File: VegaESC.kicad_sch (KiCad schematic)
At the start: 69 parts, among them J201 A, J202 B, J203 C, Q207 NTMFS5C430NLT1G, Q208 NTMFS5C430NLT1G, Q209 NTMFS5C430NLT1G, Q210 NTMFS5C430NLT1G, Q211 NTMFS5C430NLT1G, Q212 NTMFS5C430NLT1G, U201 AT32F421K8T7, U202 INA180A2, U203 FD6288Q

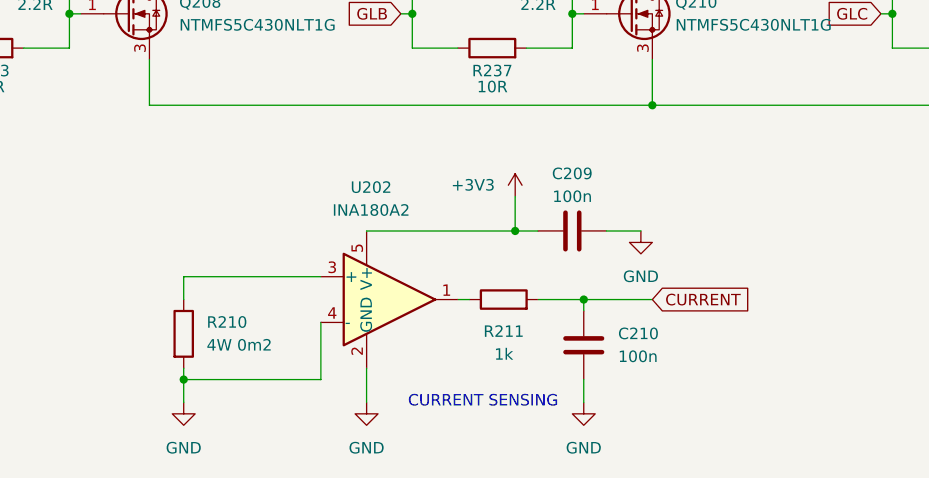
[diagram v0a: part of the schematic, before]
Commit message: esc design and current shunt resistor changes and parallel tvs diodes - still unfinished
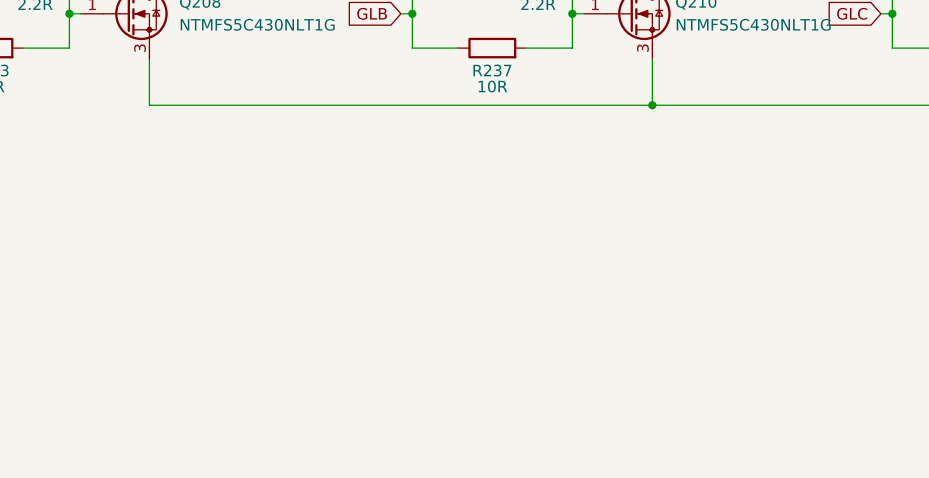
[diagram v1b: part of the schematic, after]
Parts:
- removed C209, C210: 100n, symbol Device:C
- removed R210: 4W 0m2, symbol Device:R
- removed R211: 1k, symbol Device:R
- removed U202: INA180A2, Package_TO_SOT_SMD:SOT-23-5, symbol Amplifier_Current:INA180A2
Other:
- note removed: "CURRENT SENSING"

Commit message: completed schematic design review and saved report
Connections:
- net GND: now also Q208.3 (S), Q210.3 (S), Q212.3 (S)

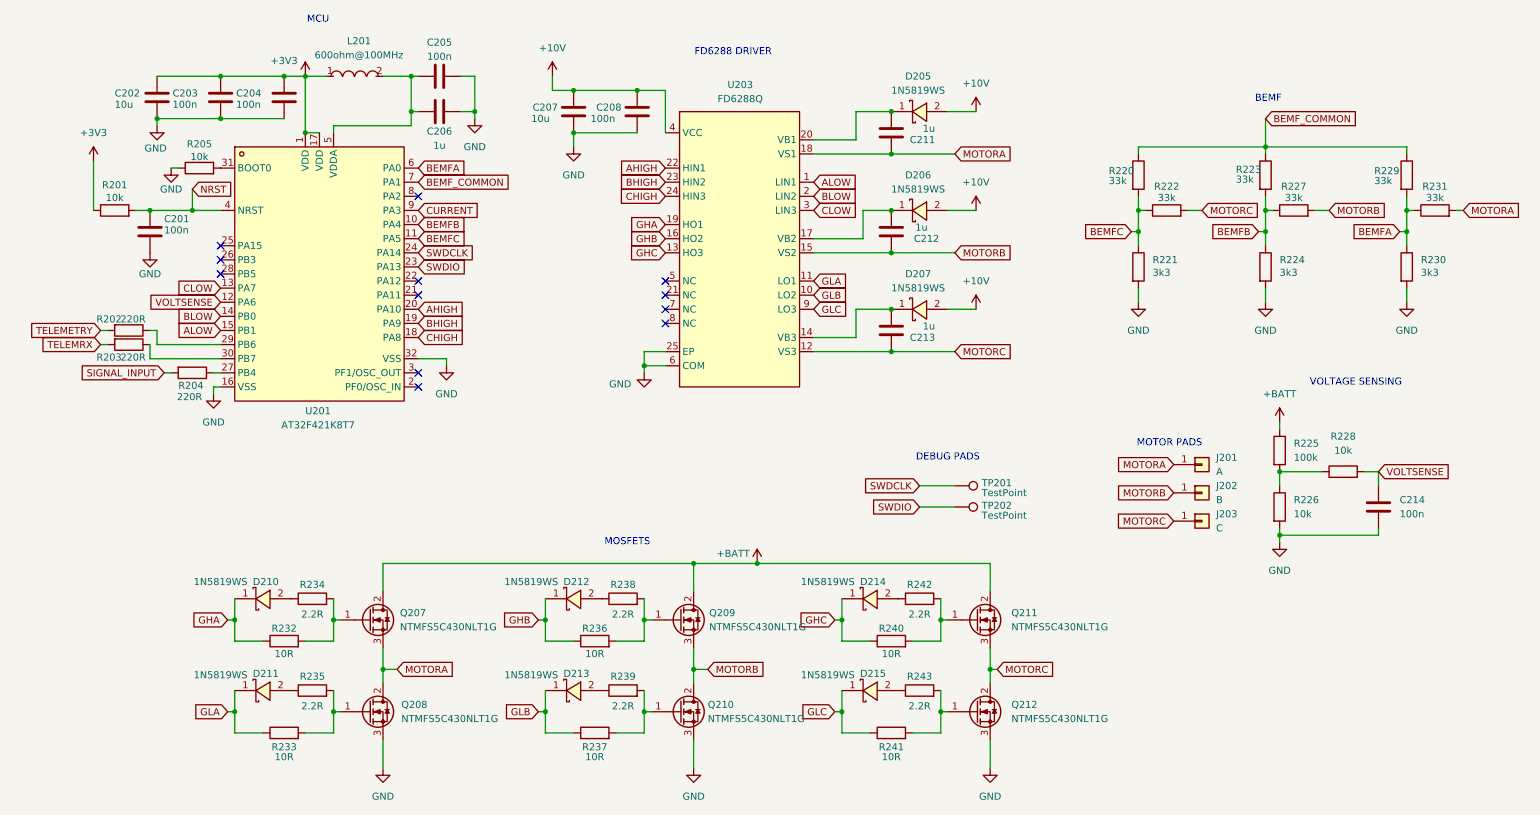
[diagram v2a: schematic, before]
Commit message: deleted voltage sensing circuit, cleaned up wires organized redid reference desginator numbers ready for pcb design
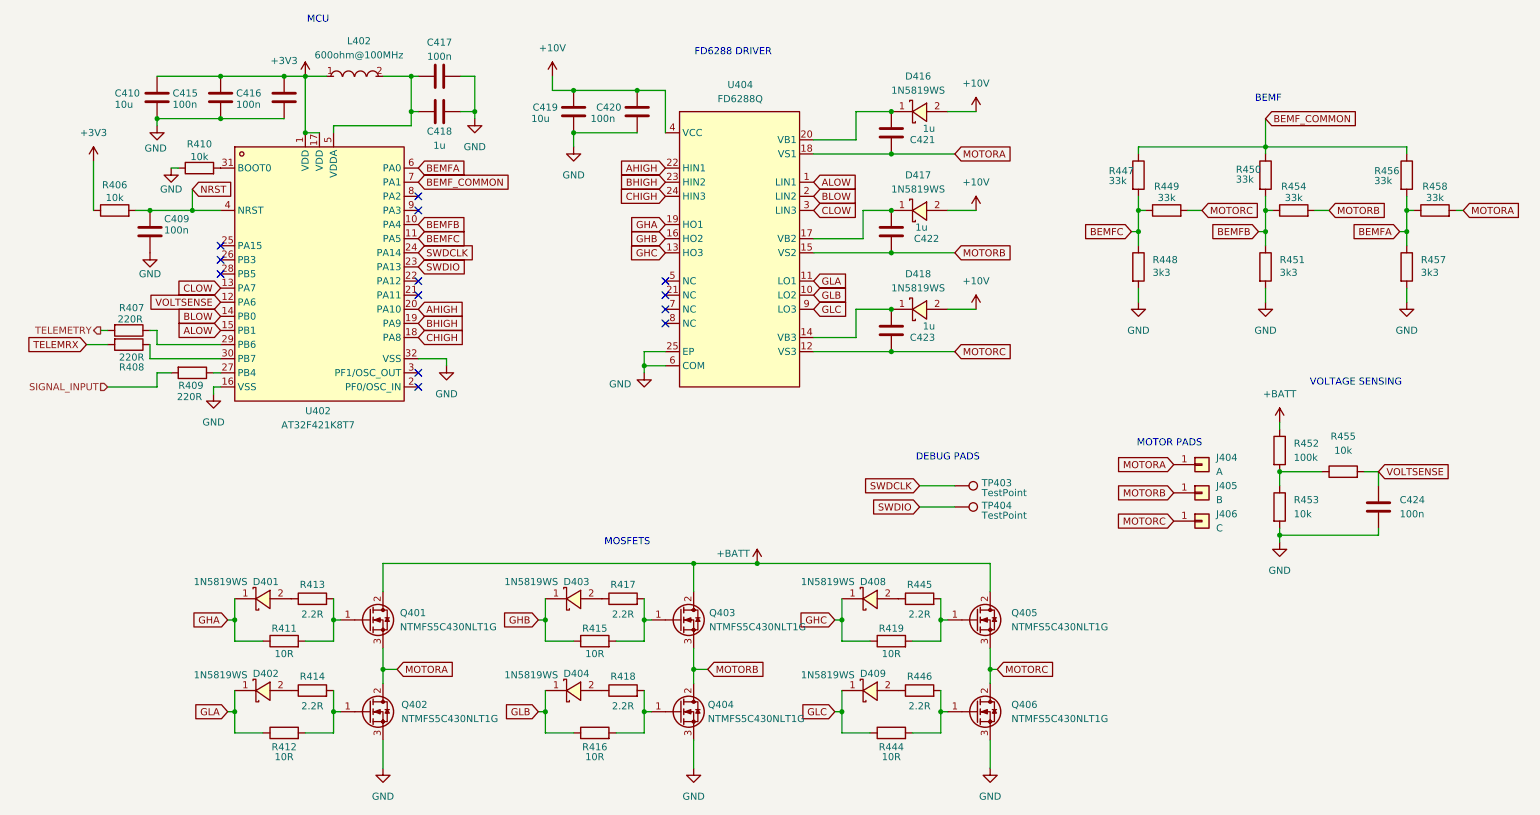
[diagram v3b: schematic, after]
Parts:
- renumbered C201 to C409, C202 to C410, C203 to C415, C204 to C416, C205 to C417, C206 to C418, C207 to C419, C208 to C420, C211 to C421, C212 to C422, C213 to C423, C214 to C424, D210 to D401, D211 to D402, D212 to D403, D213 to D404, D214 to D408, D215 to D409, D205 to D416, D206 to D417, D207 to D418, J201 to J404, J202 to J405, J203 to J406, L201 to L402, Q207 to Q401, Q208 to Q402, Q209 to Q403, Q210 to Q404, Q211 to Q405, Q212 to Q406, R201 to R406, R202 to R407, R203 to R408, R204 to R409, R205 to R410, R232 to R411, R233 to R412, R234 to R413, R235 to R414, R236 to R415, R237 to R416, R238 to R417, R239 to R418, R240 to R419, R241 to R444, R242 to R445, R243 to R446, R220 to R447, R221 to R448, R222 to R449, R223 to R450, R224 to R451, R225 to R452, R226 to R453, R227 to R454, R228 to R455, R229 to R456, R230 to R457, R231 to R458, TP201 to TP403, TP202 to TP404, U201 to U402, U203 to U404
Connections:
- net CURRENT: no longer names the net of U402.9 (PA3)
- no-connect marks 12 -> 13

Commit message: fix: assign standard footprints to all schematic components and resolve 189 missing footprint warnings
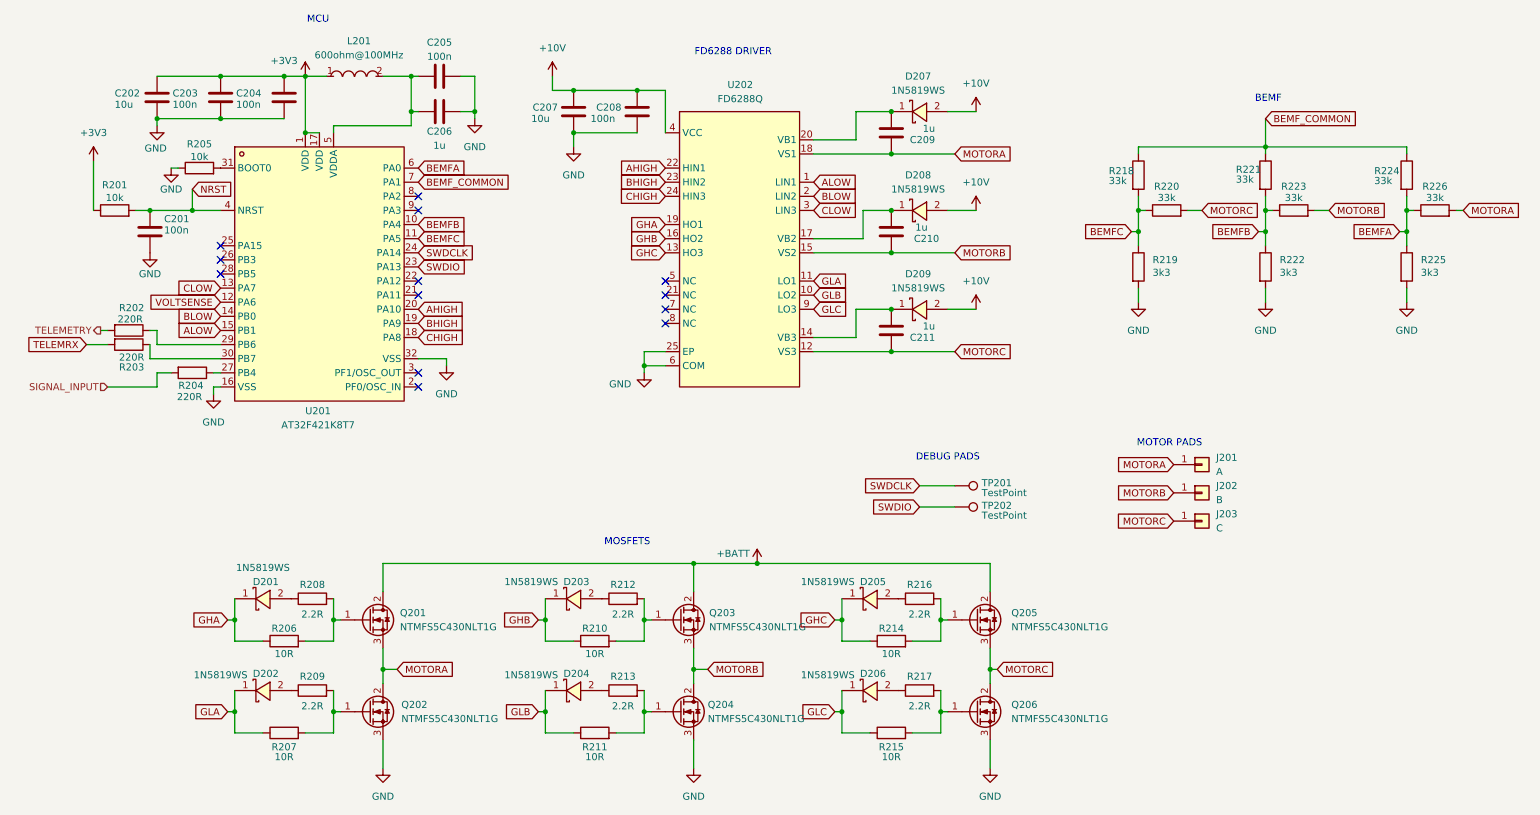
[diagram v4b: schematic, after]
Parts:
- removed C424: 100n, symbol Device:C
- removed R452: 100k, symbol Device:R
- removed R453, R455: 10k, symbol Device:R
- C201: renamed from C409; footprint (none) -> Capacitor_SMD:C_0603_1608Metric
- C202: renamed from C410; footprint (none) -> Capacitor_SMD:C_1206_3216Metric
- C203: renamed from C415; footprint (none) -> Capacitor_SMD:C_0603_1608Metric
- C204: renamed from C416; footprint (none) -> Capacitor_SMD:C_0603_1608Metric
- C205: renamed from C417; footprint (none) -> Capacitor_SMD:C_0603_1608Metric
- C206: renamed from C418; footprint (none) -> Capacitor_SMD:C_0603_1608Metric
- C207: renamed from C419; footprint (none) -> Capacitor_SMD:C_1206_3216Metric
- C208: renamed from C420; footprint (none) -> Capacitor_SMD:C_0603_1608Metric
- C209: renamed from C421; footprint (none) -> Capacitor_SMD:C_0603_1608Metric
- C210: renamed from C422; footprint (none) -> Capacitor_SMD:C_0603_1608Metric
- C211: renamed from C423; footprint (none) -> Capacitor_SMD:C_0603_1608Metric
- R202: renamed from R407; footprint (none) -> Resistor_SMD:R_0603_1608Metric
- R203: renamed from R408; footprint (none) -> Resistor_SMD:R_0603_1608Metric
- R204: renamed from R409; footprint (none) -> Resistor_SMD:R_0603_1608Metric
- R206: renamed from R411; footprint (none) -> Resistor_SMD:R_0603_1608Metric
- R207: renamed from R412; footprint (none) -> Resistor_SMD:R_0603_1608Metric
- R208: renamed from R413; footprint (none) -> Resistor_SMD:R_0603_1608Metric
- R209: renamed from R414; footprint (none) -> Resistor_SMD:R_0603_1608Metric
- R210: renamed from R415; footprint (none) -> Resistor_SMD:R_0603_1608Metric
- R211: renamed from R416; footprint (none) -> Resistor_SMD:R_0603_1608Metric
- R212: renamed from R417; footprint (none) -> Resistor_SMD:R_0603_1608Metric
- R213: renamed from R418; footprint (none) -> Resistor_SMD:R_0603_1608Metric
- R214: renamed from R419; footprint (none) -> Resistor_SMD:R_0603_1608Metric
- R215: renamed from R444; footprint (none) -> Resistor_SMD:R_0603_1608Metric
- R216: renamed from R445; footprint (none) -> Resistor_SMD:R_0603_1608Metric
- R217: renamed from R446; footprint (none) -> Resistor_SMD:R_0603_1608Metric
- R218: renamed from R447; footprint (none) -> Resistor_SMD:R_0603_1608Metric
- R219: renamed from R448; footprint (none) -> Resistor_SMD:R_0603_1608Metric
- R220: renamed from R449; footprint (none) -> Resistor_SMD:R_0603_1608Metric
- R221: renamed from R450; footprint (none) -> Resistor_SMD:R_0603_1608Metric
- R222: renamed from R451; footprint (none) -> Resistor_SMD:R_0603_1608Metric
- R223: renamed from R454; footprint (none) -> Resistor_SMD:R_0603_1608Metric
- R224: renamed from R456; footprint (none) -> Resistor_SMD:R_0603_1608Metric
- R225: renamed from R457; footprint (none) -> Resistor_SMD:R_0603_1608Metric
- R226: renamed from R458; footprint (none) -> Resistor_SMD:R_0603_1608Metric
- TP201: renamed from TP403; footprint (none) -> TestPoint:TestPoint_Pad_D1.0mm
- TP202: renamed from TP404; footprint (none) -> TestPoint:TestPoint_Pad_D1.0mm
- renumbered D401 to D201, D402 to D202, D403 to D203, D404 to D204, D408 to D205, D409 to D206, D416 to D207, D417 to D208, D418 to D209, J404 to J201, J405 to J202, J406 to J203, L402 to L201, Q401 to Q201, Q402 to Q202, Q403 to Q203, Q404 to Q204, Q405 to Q205, Q406 to Q206, R406 to R201, R410 to R205, U402 to U201, U404 to U202
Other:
- note removed: "VOLTAGE SENSING"

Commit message: Refactor schematic: update MCU to AT32F421G8U7 (QFN-28), update footprints, and re-annotate designators
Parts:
- removed C201, C203, C204, C205: 100n, Capacitor_SMD:C_0603_1608Metric, symbol Device:C
- removed C202: 10u, Capacitor_SMD:C_1206_3216Metric, symbol Device:C
- removed C206: 1u, Capacitor_SMD:C_0603_1608Metric, symbol Device:C
- removed L201: 600ohm@100MHz, easyeda2kicad:L0603, symbol easyeda2kicad:GZ1608D601TF
- removed R201, R205: 10k, Resistor_SMD:R_0603_1608Metric, symbol Device:R
- removed R202, R203, R204: 220R, Resistor_SMD:R_0603_1608Metric, symbol Device:R
- removed U201: AT32F421K8T7, easyeda2kicad:LQFP-32_L7.0-W7.0-P0.80-LS9.0-BL, symbol easyeda2kicad:AT32F421K8T7_C3029575
- added C212, C214, C215, C216: 100n, Capacitor_SMD:C_0603_1608Metric, symbol Device:C
- added C213: 10u, Capacitor_SMD:C_1206_3216Metric, symbol Device:C
- added C217: 1u, Capacitor_SMD:C_0603_1608Metric, symbol Device:C
- added L202: 600ohm@100MHz, easyeda2kicad:L0603, symbol easyeda2kicad:GZ1608D601TF
- added R227, R231: 10k, Resistor_SMD:R_0603_1608Metric, symbol Device:R
- added R228, R230: 220R, Resistor_SMD:R_0603_1608Metric, symbol Device:R
- added U203: AT32F421G8U7, easyeda2kicad:QFN-28_L4.0-W4.0-P0.40-TL-EP2.4, symbol easyeda2kicad:AT32F421G8U7
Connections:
- net +3V3: now also C213.1, C214.1, C215.1, L202.1, R227.1, U203.17 (VDD)
- net AHIGH: now also U203.20 (PA10)
- net ALOW: now also U203.15 (PB1)
- net BEMFA: now also U203.6 (PA0)
- net BEMFB: now also U203.10 (PA4)
- net BEMFC: now also U203.11 (PA5)
- net BEMF_COMMON: now also U203.7 (PA1)
- net BHIGH: now also U203.19 (PA9)
- net BLOW: now also U203.14 (PB0)
- net CHIGH: now also U203.18 (PA8)
- net CLOW: now also U203.13 (PA7)
- net GND: now also C212.2, C213.2, C214.2, C215.2, C216.2, C217.2, R231.1, U203.16 (VSS), U203.29 (VSS)
- net NRST: now also C212.1, R227.2, U203.4 (NRST)
- net SIGNAL_INPUT: now also R230.2
- net SWDCLK: now also U203.22 (PA14)
- net SWDIO: now also U203.21 (PA13)
- net TELEMETRY: now also R228.2
- new net: R228.1, U203.27 (PB6)
- new net: C216.1, C217.1, L202.2, U203.5 (VDDA)
- new net: R230.1, U203.25 (PB4)
- new net: R231.2, U203.1 (BOOT0)
- no-connect marks 13 -> 14
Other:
- moved on the sheet: J201, J202, J203, TP201, TP202
